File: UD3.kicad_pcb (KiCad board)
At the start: 4 copper layers, 99.8 x 99.8 mm, 185 parts, among them J1 LED_CON2, J10 HR911105A, J11 USB_B_Micro, J12 Prog, J13 RLY, J14 GDT2, J15 Conn_02x04_Odd_Even, J16 CT, J2 LED_CON1, J3 THERM, J4 UMEAS, J5 GDT2, J6 GDT1, J7 IBUS, J8 RLY, J9 CT, U1 CY8C5868AXI-LP035, U10 AMS1117-3.3, U11 IPS4260L, U12 TC7662Bx0A, U13 ULN2003LV, U14 LM7812_TO220, U15 LM7805_TO220, U2 MIC4426, U3 TL082, U4 MIC4426, U5 DMC3021LK4, U6 DMC3021LK4, U7 DMC3021LK4, U8 DMC3021LK4, U9 W5500

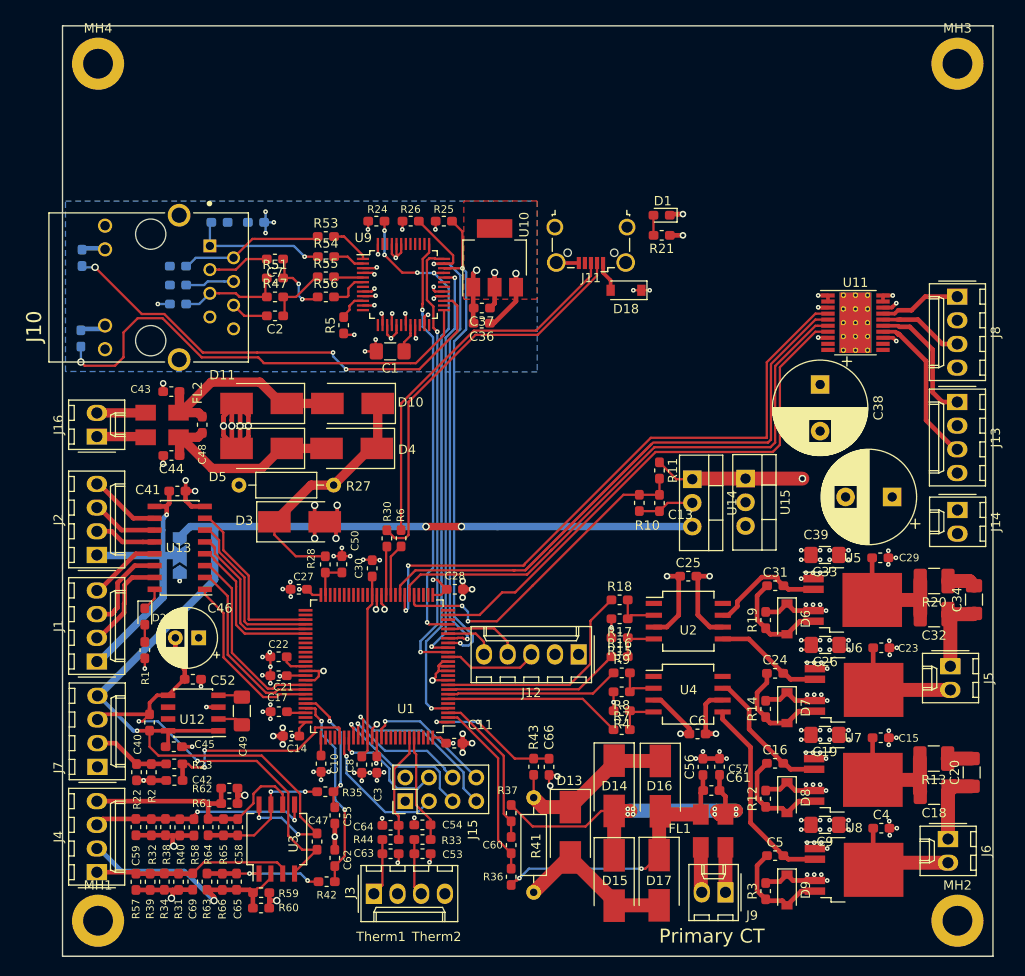
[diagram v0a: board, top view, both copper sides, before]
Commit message: Removed W5500
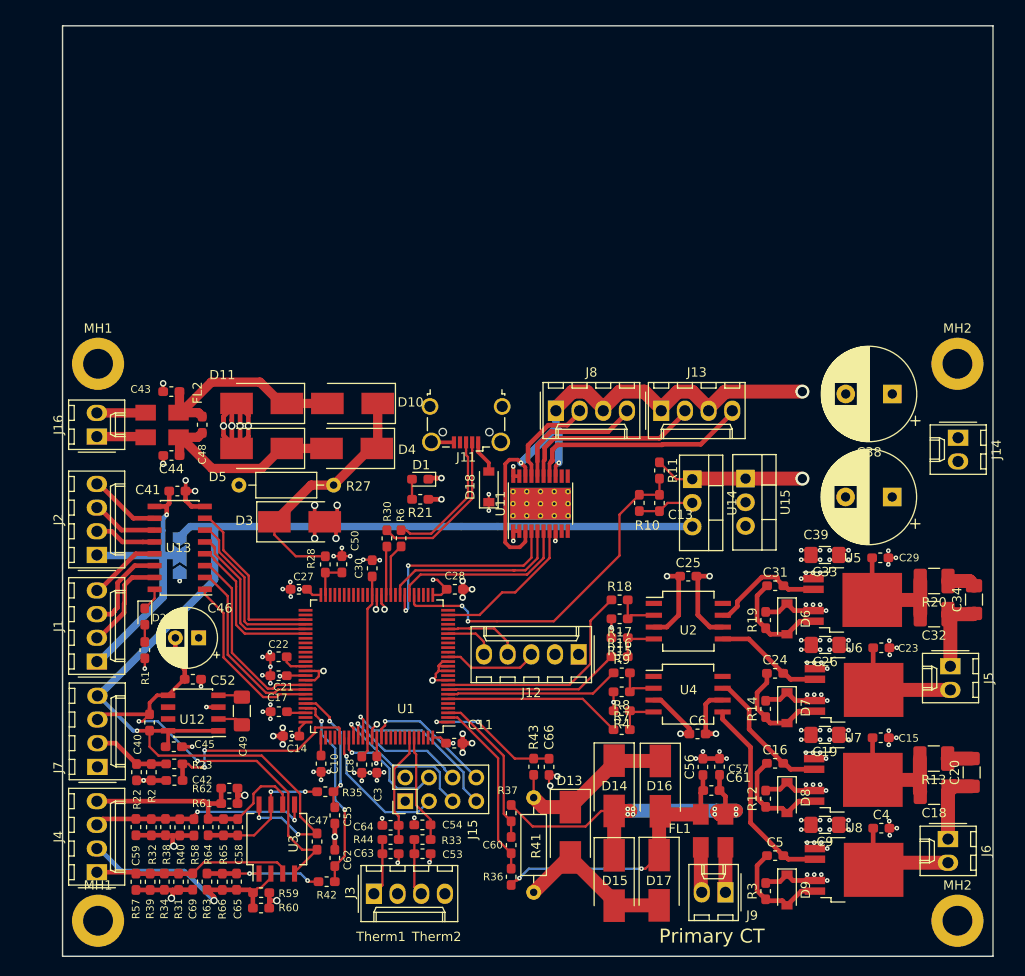
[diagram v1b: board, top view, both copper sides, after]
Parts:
- removed C1: 4µ7, Capacitor_SMD:C_1206_3216Metric_Pad1.42x1.75mm_HandSolder
- removed C12: 10nF, Capacitor_SMD:C_0603_1608Metric_Pad1.05x0.95mm_HandSolder
- removed C2, C7: 6,8nF, Capacitor_SMD:C_0603_1608Metric_Pad1.05x0.95mm_HandSolder
- removed C35: 22nF, Capacitor_SMD:C_0603_1608Metric_Pad1.05x0.95mm_HandSolder
- removed C36, C37: 100nF, Capacitor_SMD:C_0603_1608Metric_Pad1.05x0.95mm_HandSolder
- removed J10: HR911105A, HanRun:HANRUN_HR911105A
- removed MH3, MH4: MountingHole_Pad, MountingHole:MountingHole_3.2mm_M3_DIN965_Pad
- removed R24, R25, R26: 1k, Resistor_SMD:R_0603_1608Metric_Pad1.05x0.95mm_HandSolder
- removed R45: 10, Resistor_SMD:R_0603_1608Metric_Pad1.05x0.95mm_HandSolder
- removed R47, R48, R51, R52: 49,9, Resistor_SMD:R_0603_1608Metric_Pad1.05x0.95mm_HandSolder
- removed R49, R50: 330, Resistor_SMD:R_0603_1608Metric_Pad1.05x0.95mm_HandSolder
- removed R5: 12,4k, Resistor_SMD:R_0603_1608Metric_Pad1.05x0.95mm_HandSolder
- removed R53, R54, R55, R56: 33, Resistor_SMD:R_0603_1608Metric_Pad1.05x0.95mm_HandSolder
- removed U10: AMS1117-3.3, Package_TO_SOT_SMD:SOT-223-3_TabPin2
- removed U9: W5500, Package_QFP:TQFP-48_7x7mm_P0.5mm
- added MH1: MountingHole_Pad, MountingHole:MountingHole_3.2mm_M3_DIN965_Pad, F.Cu at (151.1, 98.2)
- added MH2: MountingHole_Pad, MountingHole:MountingHole_3.2mm_M3_DIN965_Pad, F.Cu at (243.3, 98.2)
- moved J8 44.8 mm to (200.3, 103.3), turned to 0 degrees
- moved U11 39.0 mm to (198.6, 113.2), turned to 90 degrees
- moved R21 38.4 mm to (185.7, 112.8)
- moved D1 38.4 mm to (185.7, 110.6)
- moved J13 31.8 mm to (211.6, 103.3), turned to 0 degrees
- moved D18 25.7 mm to (193.1, 111.4), turned to 90 degrees
- moved J11 23.4 mm to (190.6, 104.8)
- moved C38 7.81 mm to (236.3, 101.5), turned to 180 degrees
- moved J14 7.75 mm to (243.4, 106.2)
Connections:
- J13 pad 1: Net-(J13-Pad1) -> +24V
- J13 pad 2: GND -> Net-(J13-Pad2)
- J13 pad 3: Net-(J13-Pad3) -> +24V
- J13 pad 4: GND -> Net-(J13-Pad4)
- J8 pad 1: Net-(J8-Pad1) -> +24V
- J8 pad 2: GND -> Net-(J8-Pad2)
- J8 pad 3: Net-(J8-Pad3) -> +24V
- J8 pad 4: GND -> Net-(J8-Pad4)
- U11 pad 14: Net-(J13-Pad3) -> Net-(J13-Pad4)
- U11 pad 15: Net-(J13-Pad1) -> Net-(J13-Pad2)
- U11 pad 16: Net-(J8-Pad3) -> Net-(J8-Pad4)
- U11 pad 17: Net-(J8-Pad1) -> Net-(J8-Pad2)
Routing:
- net Relay2: track 82.6 -> 20.0 mm
- net ETH_SCLK: track 61.2 -> 0.03 mm, vias 5 -> 0
- net +24V: track 76.8 -> 134.1 mm
- net ETH_MOSI: track 53.8 -> 0.00 mm, vias 2 -> 0
- net ETH_MISO: track 52.8 -> 0.00 mm, vias 2 -> 0
- net ACTLED: track 51.1 -> 0.00 mm, vias 3 -> 0
- net LINKLED: track 50.2 -> 0.00 mm, vias 1 -> 0
- net ETH_INT: track 48.1 -> 0.03 mm, vias 2 -> 0
- net Relay1: track 67.7 -> 23.1 mm
- net ETH_RST: track 44.0 -> 0.00 mm, vias 2 -> 0
- net ETH_CS: track 43.6 -> 0.00 mm, vias 2 -> 0
- net FAN: track 62.4 -> 19.5 mm
- net Relay3: track 58.2 -> 16.3 mm
- net GND: track 243.2 -> 215.9 mm, vias 139 -> 120
- net Net-(J11-Pad2): track 44.3 -> 17.3 mm
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- removed copper zone on B.Cu, net +3V3
- removed copper zone on F.Cu, net +3V3
